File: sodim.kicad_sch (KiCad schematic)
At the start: 7 parts, among them J1 Edge_Conn_Bus_LPDDR5_testbed, J2 Edge_Connus_LPDDR5_testbed, U7 AT24CS01_SOT23

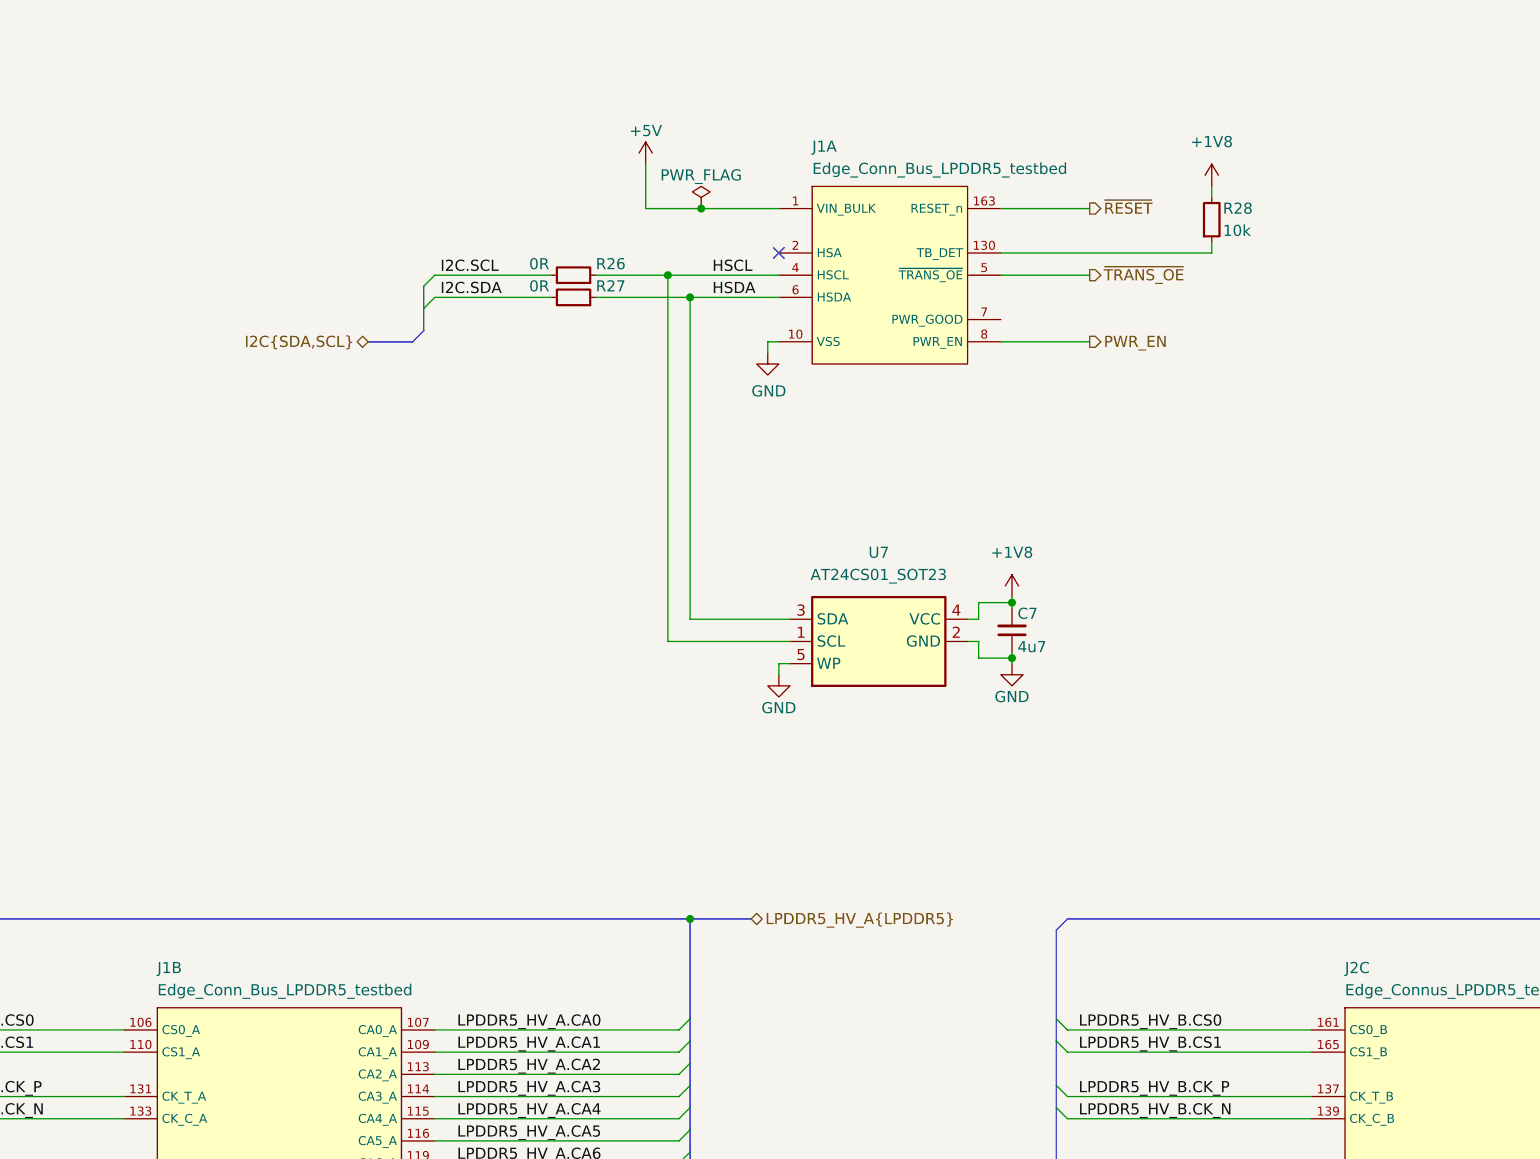
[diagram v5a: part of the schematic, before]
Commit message: [#52835] schematics: update translators pinout to for better package breakout
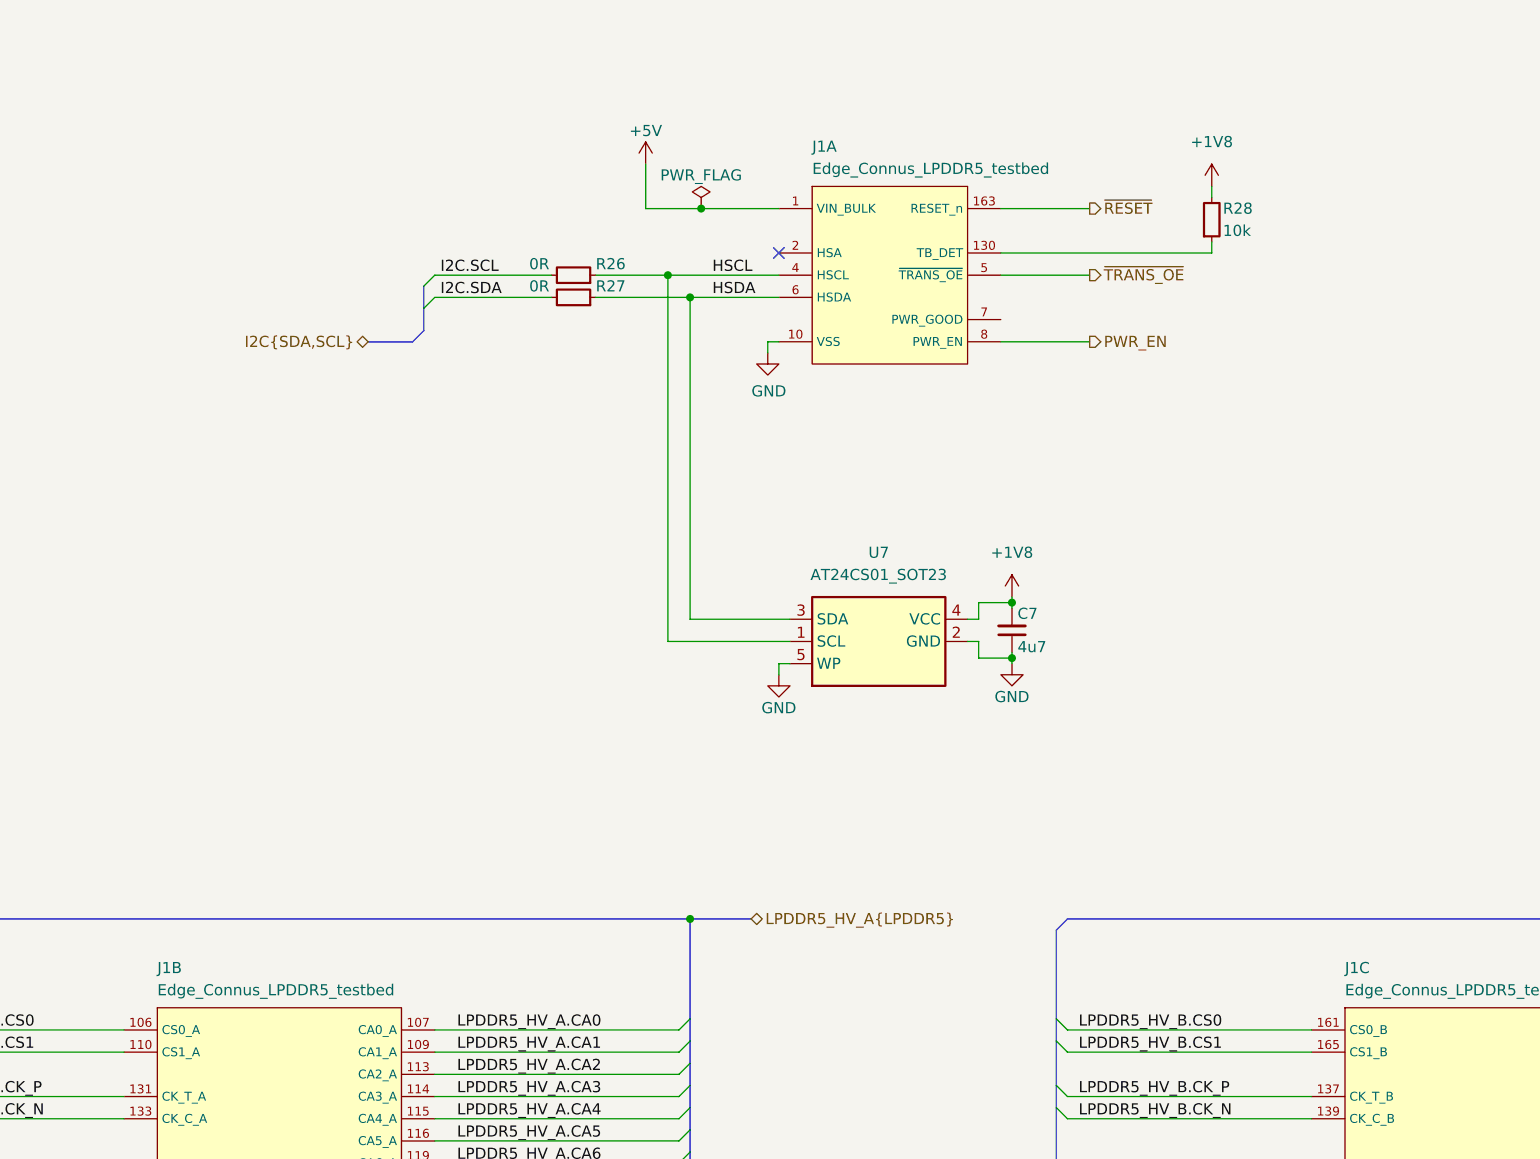
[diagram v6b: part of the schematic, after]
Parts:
- J1: value Edge_Conn_Bus_LPDDR5_testbed -> Edge_Connus_LPDDR5_testbed
- renumbered J2 to J1
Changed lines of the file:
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@@
       (effects (font (size 1.27 1.27)) (justify left bottom))
     )
-    (property "Value" "Edge_Conn_Bus_LPDDR5_testbed" (id 1) (at 121.92 139.7 0)
+    (property "Value" "Edge_Connus_LPDDR5_testbed" (id 1) (at 121.92 139.7 0)
       (effects (font (size 1.27 1.27)) (justify left bottom))
     )
@@
   (symbol (lib_id "antmicroMemoryConnectorsPCCardSockets:Edge_Conn_Bus_LPDDR5_testbed") (at 254 143.51 0) (unit 3)
     (in_bom yes) (on_board yes)
-    (property "Reference" "J2" (id 0) (at 257.81 137.16 0)
+    (property "Reference" "J1" (id 0) (at 257.81 137.16 0)
       (effects (font (size 1.27 1.27)) (justify left bottom))
     )
@@
       (effects (font (size 1.27 1.27)) (justify left bottom))
     )
-    (property "Value" "Edge_Conn_Bus_LPDDR5_testbed" (id 1) (at 196.85 45.72 0)
+    (property "Value" "Edge_Connus_LPDDR5_testbed" (id 1) (at 196.85 45.72 0)
       (effects (font (size 1.27 1.27)) (justify left bottom))
     )

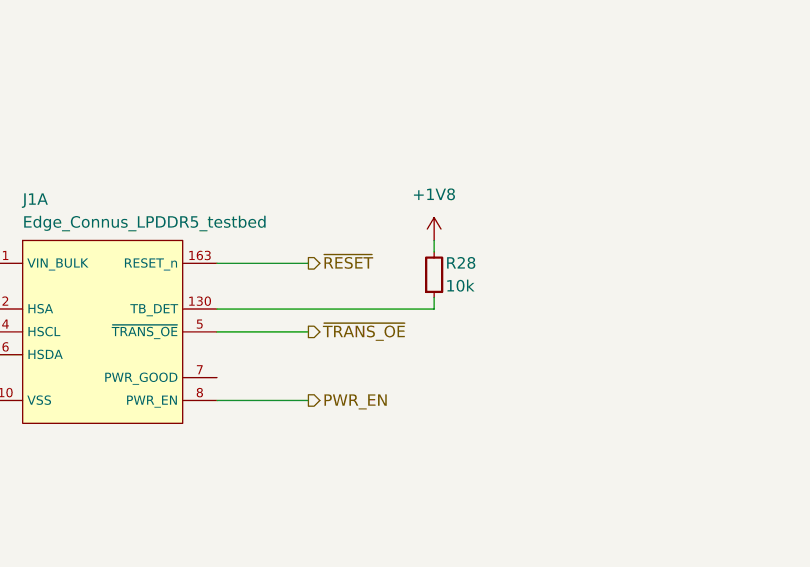
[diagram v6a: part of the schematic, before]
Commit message: [#52536] schematics: use voltage divider to detect pin
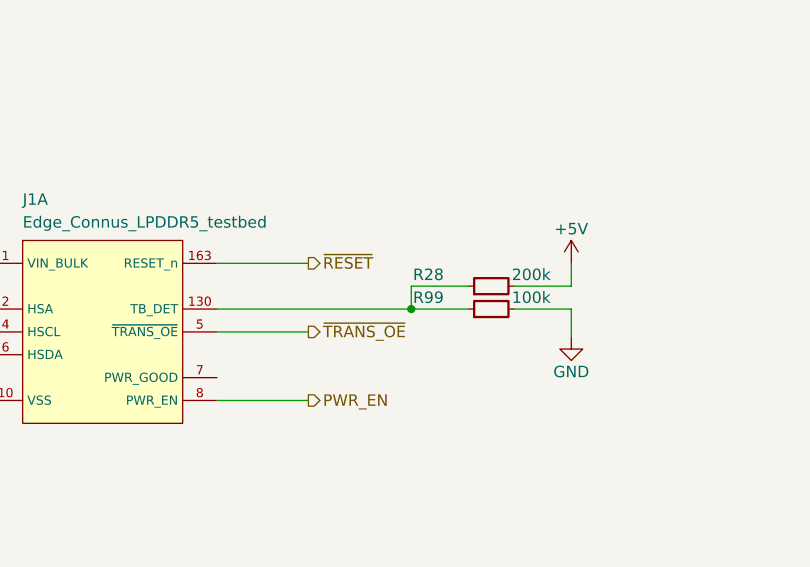
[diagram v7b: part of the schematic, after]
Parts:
- removed R28: R_10k_0402, antmicro-footprints:R_0402_1005Metric, symbol antmicroResistors0402:R_10k_0402
- added R28: R_200k_0402, antmicro-footprints:R_0402_1005Metric, symbol antmicroResistors0402:R_200k_0402
- added R99: R_100k_0402, antmicro-footprints:R_0402_1005Metric, symbol antmicroResistors0402:R_100k_0402
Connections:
- net +5V: now also R28.2
- net GND: now also R99.2
- net at J1.130 (TB_DET): now also R28.1, R99.1

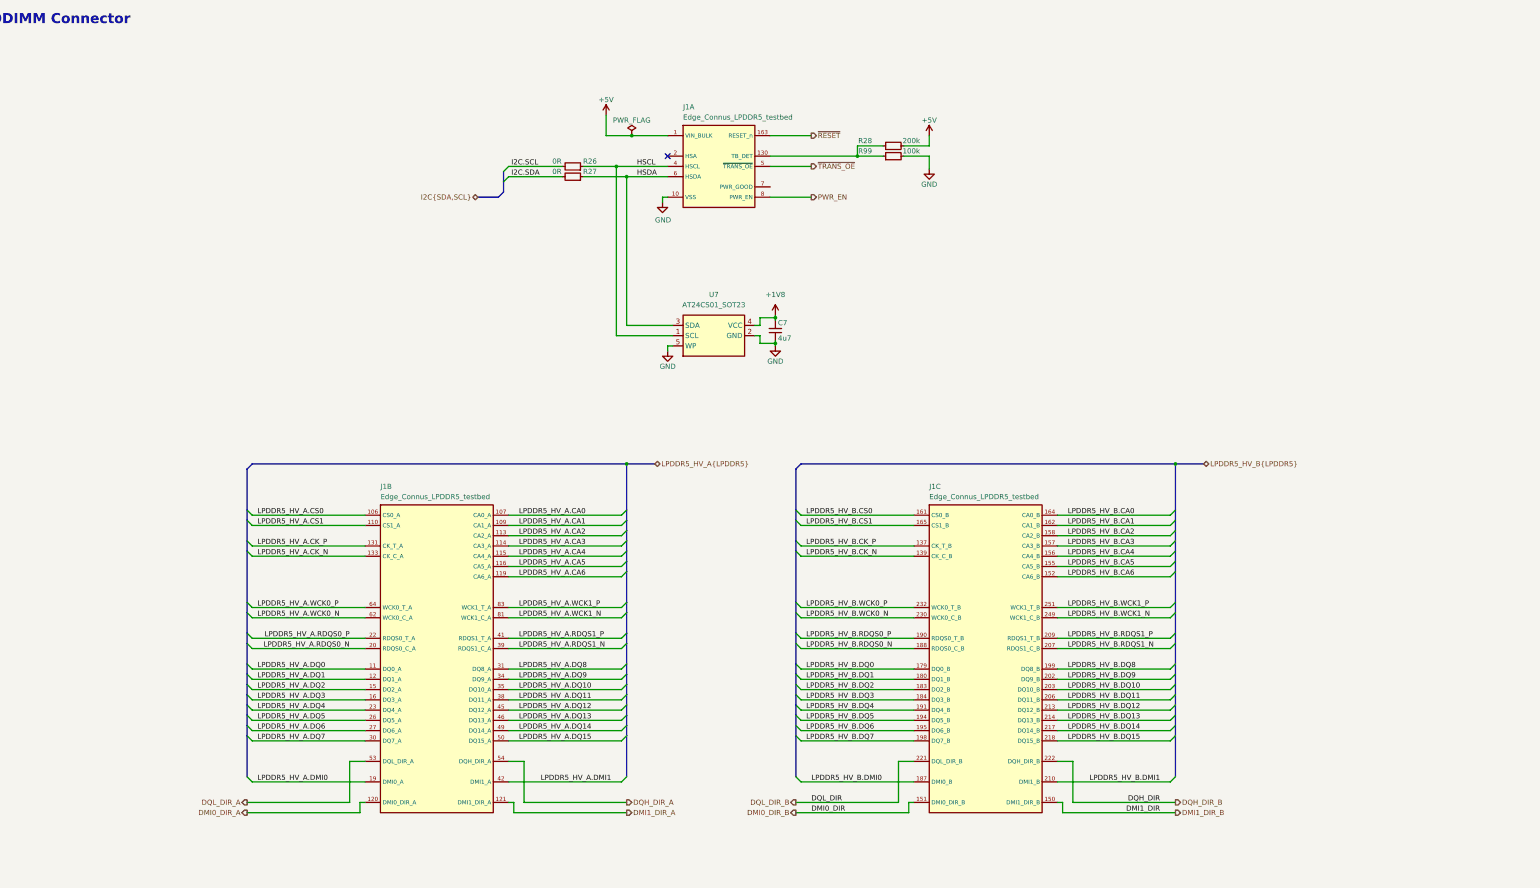
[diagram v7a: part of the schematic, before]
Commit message: [#52536] 52835: use resistors dividers instead of translators
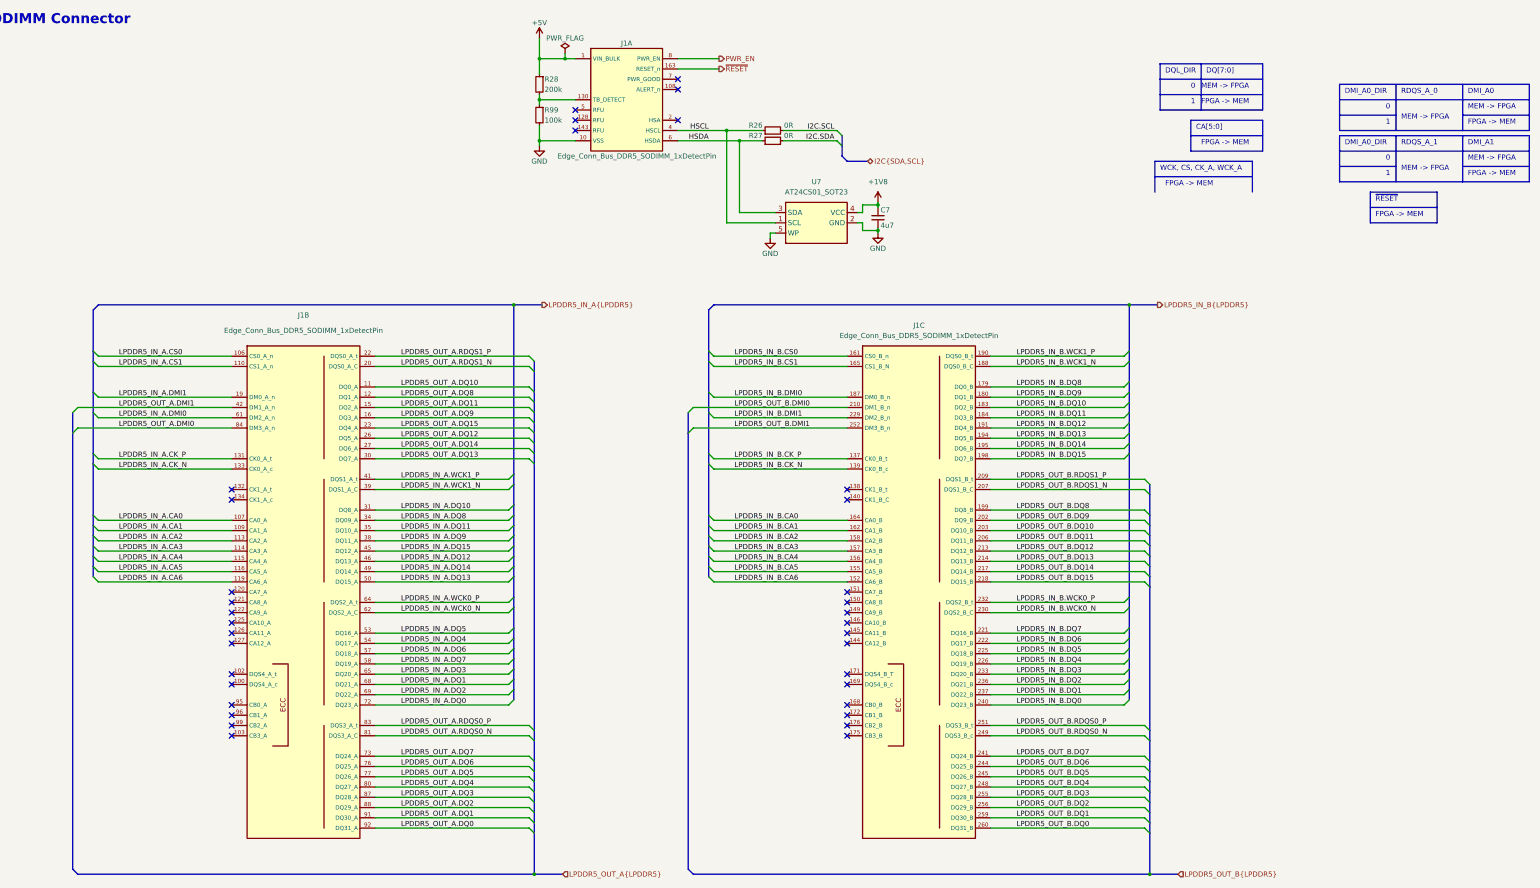
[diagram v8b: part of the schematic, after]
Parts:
- removed J1: Edge_Connus_LPDDR5_testbed, antmicro-footprints:Edge_Conn_Bus_DDR5_SODIMM, symbol antmicroMemoryConnectorsPCCardSockets:Edge_Conn_Bus_LPDDR5_testbed
- added J1: Edge_Conn_Bus_DDR5_SODIMM_1xDetectPin, antmicro-footprints:Edge_Conn_Bus_DDR5_SODIMM, symbol antmicroMemoryConnectorsPCCardSockets:Edge_Conn_Bus_DDR5_SODIMM_1xDetectPin
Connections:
- net +5V: now also R28.1, J1.1 (VIN_BULK), J1.3 (VIN_BULK); no longer R28.2
- net GND: now also J1.10 (VSS), J1.101 (VSS), J1.104 (VSS), J1.105 (VSS), J1.111 (VSS), J1.112 (VSS), J1.117 (VSS), J1.118 (VSS), J1.123 (VSS), J1.124 (VSS), J1.129 (VSS), J1.13 (VSS), J1.135 (VSS), J1.136 (VSS), J1.14 (VSS), J1.141 (VSS), J1.142 (VSS), J1.147 (VSS), J1.148 (VSS), J1.153 (VSS), J1.154 (VSS), J1.159 (VSS), J1.160 (VSS), J1.166 (VSS), J1.167 (VSS), J1.17 (VSS), J1.170 (VSS), J1.173 (VSS), J1.174 (VSS), J1.177 (VSS), J1.178 (VSS), J1.18 (VSS), J1.181 (VSS), J1.182 (VSS), J1.185 (VSS), J1.186 (VSS), J1.189 (VSS), J1.192 (VSS), J1.193 (VSS), J1.196 (VSS), J1.197 (VSS), J1.200 (VSS), J1.201 (VSS), J1.204 (VSS), J1.205 (VSS), J1.208 (VSS), J1.21 (VSS), J1.211 (VSS), J1.212 (VSS), J1.215 (VSS), J1.216 (VSS), J1.219 (VSS), J1.220 (VSS), J1.223 (VSS), J1.224 (VSS), J1.227 (VSS), J1.228 (VSS), J1.231 (VSS), J1.234 (VSS), J1.235 (VSS), J1.238 (VSS), J1.239 (VSS), J1.24 (VSS), J1.242 (VSS), J1.243 (VSS), J1.246 (VSS), J1.247 (VSS), J1.25 (VSS), J1.250 (VSS), J1.253 (VSS), J1.254 (VSS), J1.257 (VSS), J1.258 (VSS), J1.261 (VSS), J1.262 (VSS), J1.28 (VSS), J1.29 (VSS), J1.32 (VSS), J1.33 (VSS), J1.36 (VSS), J1.37 (VSS), J1.40 (VSS), J1.43 (VSS), J1.44 (VSS), J1.47 (VSS), J1.48 (VSS), J1.51 (VSS), J1.52 (VSS), J1.55 (VSS), J1.56 (VSS), J1.59 (VSS), J1.60 (VSS), J1.63 (VSS), J1.66 (VSS), J1.67 (VSS), J1.70 (VSS), J1.71 (VSS), J1.74 (VSS), J1.75 (VSS), J1.78 (VSS), J1.79 (VSS), J1.82 (VSS), J1.85 (VSS), J1.86 (VSS), J1.89 (VSS), J1.9 (VSS), J1.90 (VSS), J1.93 (VSS), J1.94 (VSS), J1.97 (VSS), J1.98 (VSS)
- net HSCL: now also J1.4 (HSCL)
- net HSDA: now also J1.6 (HSDA)
- net PWR_EN: now also J1.8 (PWR_EN)
- net ~{RESET}: now also J1.163 (RESET_n)
- net at R99.1: now also R28.2, J1.130 (TB_DETECT); no longer R28.1
- new net LPDDR5_IN_A.CA0: J1.107 (CA0_A)
- new net LPDDR5_IN_A.CA1: J1.109 (CA1_A)
- new net LPDDR5_IN_A.CA2: J1.113 (CA2_A)
- new net LPDDR5_IN_A.CA3: J1.114 (CA3_A)
- new net LPDDR5_IN_A.CA4: J1.115 (CA4_A)
- new net LPDDR5_IN_A.CA5: J1.116 (CA5_A)
- new net LPDDR5_IN_A.CA6: J1.119 (CA6_A)
- new net LPDDR5_IN_A.CK_N: J1.133 (CK0_A_c)
- new net LPDDR5_IN_A.CK_P: J1.131 (CK0_A_t)
- new net LPDDR5_IN_A.CS0: J1.106 (CS0_A_n)
- new net LPDDR5_IN_A.CS1: J1.110 (CS1_A_n)
- new net LPDDR5_IN_A.DMI0: J1.61 (DM2_A_n)
- new net LPDDR5_IN_A.DMI1: J1.19 (DM0_A_n)
- new net LPDDR5_IN_A.DQ0: J1.72 (DQ23_A)
- new net LPDDR5_IN_A.DQ1: J1.68 (DQ21_A)
- new net LPDDR5_IN_A.DQ10: J1.31 (DQ8_A)
- new net LPDDR5_IN_A.DQ11: J1.35 (DQ10_A)
- new net LPDDR5_IN_A.DQ12: J1.46 (DQ13_A)
- new net LPDDR5_IN_A.DQ13: J1.50 (DQ15_A)
- new net LPDDR5_IN_A.DQ14: J1.49 (DQ14_A)
- new net LPDDR5_IN_A.DQ15: J1.45 (DQ12_A)
- new net LPDDR5_IN_A.DQ2: J1.69 (DQ22_A)
- new net LPDDR5_IN_A.DQ3: J1.65 (DQ20_A)
- new net LPDDR5_IN_A.DQ4: J1.54 (DQ17_A)
- new net LPDDR5_IN_A.DQ5: J1.53 (DQ16_A)
- new net LPDDR5_IN_A.DQ6: J1.57 (DQ18_A)
- new net LPDDR5_IN_A.DQ7: J1.58 (DQ19_A)
- new net LPDDR5_IN_A.DQ8: J1.34 (DQ09_A)
- new net LPDDR5_IN_A.DQ9: J1.38 (DQ11_A)
- new net LPDDR5_IN_A.WCK0_N: J1.62 (DQS2_A_C)
- new net LPDDR5_IN_A.WCK0_P: J1.64 (DQS2_A_t)
- new net LPDDR5_IN_A.WCK1_N: J1.39 (DQS1_A_C)
- new net LPDDR5_IN_A.WCK1_P: J1.41 (DQS1_A_t)
- new net LPDDR5_IN_B.CA0: J1.164 (CA0_B)
- new net LPDDR5_IN_B.CA1: J1.162 (CA1_B)
- new net LPDDR5_IN_B.CA2: J1.158 (CA2_B)
- new net LPDDR5_IN_B.CA3: J1.157 (CA3_B)
- new net LPDDR5_IN_B.CA4: J1.156 (CA4_B)
- new net LPDDR5_IN_B.CA5: J1.155 (CA5_B)
- new net LPDDR5_IN_B.CA6: J1.152 (CA6_B)
- new net LPDDR5_IN_B.CK_N: J1.139 (CK0_B_c)
- new net LPDDR5_IN_B.CK_P: J1.137 (CK0_B_t)
- new net LPDDR5_IN_B.CS0: J1.161 (CS0_B_n)
- new net LPDDR5_IN_B.CS1: J1.165 (CS1_B_N)
- new net LPDDR5_IN_B.DMI0: J1.187 (DM0_B_n)
- new net LPDDR5_IN_B.DMI1: J1.229 (DM2_B_n)
- new net LPDDR5_IN_B.DQ0: J1.240 (DQ23_B)
- new net LPDDR5_IN_B.DQ1: J1.237 (DQ22_B)
- new net LPDDR5_IN_B.DQ10: J1.183 (DQ2_B)
- new net LPDDR5_IN_B.DQ11: J1.184 (DQ3_B)
- new net LPDDR5_IN_B.DQ12: J1.191 (DQ4_B)
- new net LPDDR5_IN_B.DQ13: J1.194 (DQ5_B)
- new net LPDDR5_IN_B.DQ14: J1.195 (DQ6_B)
- new net LPDDR5_IN_B.DQ15: J1.198 (DQ7_B)
- new net LPDDR5_IN_B.DQ2: J1.236 (DQ21_B)
- new net LPDDR5_IN_B.DQ3: J1.233 (DQ20_B)
- new net LPDDR5_IN_B.DQ4: J1.226 (DQ19_B)
- new net LPDDR5_IN_B.DQ5: J1.225 (DQ18_B)
- new net LPDDR5_IN_B.DQ6: J1.222 (DQ17_B)
- new net LPDDR5_IN_B.DQ7: J1.221 (DQ16_B)
- new net LPDDR5_IN_B.DQ8: J1.179 (DQ0_B)
- new net LPDDR5_IN_B.DQ9: J1.180 (DQ1_B)
- new net LPDDR5_IN_B.WCK0_N: J1.230 (DQS2_B_C)
- new net LPDDR5_IN_B.WCK0_P: J1.232 (DQS2_B_t)
- new net LPDDR5_IN_B.WCK1_N: J1.188 (DQS0_B_C)
- new net LPDDR5_IN_B.WCK1_P: J1.190 (DQS0_B_t)
- new net LPDDR5_OUT_A.DMI0: J1.84 (DM3_A_n)
- new net LPDDR5_OUT_A.DMI1: J1.42 (DM1_A_n)
- new net LPDDR5_OUT_A.DQ0: J1.92 (DQ31_A)
- new net LPDDR5_OUT_A.DQ1: J1.91 (DQ30_A)
- new net LPDDR5_OUT_A.DQ10: J1.11 (DQ0_A)
- new net LPDDR5_OUT_A.DQ11: J1.15 (DQ2_A)
- new net LPDDR5_OUT_A.DQ12: J1.26 (DQ5_A)
- new net LPDDR5_OUT_A.DQ13: J1.30 (DQ7_A)
- new net LPDDR5_OUT_A.DQ14: J1.27 (DQ6_A)
- new net LPDDR5_OUT_A.DQ15: J1.23 (DQ4_A)
- new net LPDDR5_OUT_A.DQ2: J1.88 (DQ29_A)
- new net LPDDR5_OUT_A.DQ3: J1.87 (DQ28_A)
- new net LPDDR5_OUT_A.DQ4: J1.80 (DQ27_A)
- new net LPDDR5_OUT_A.DQ5: J1.77 (DQ26_A)
- new net LPDDR5_OUT_A.DQ6: J1.76 (DQ25_A)
- new net LPDDR5_OUT_A.DQ7: J1.73 (DQ24_A)
- new net LPDDR5_OUT_A.DQ8: J1.12 (DQ1_A)
- new net LPDDR5_OUT_A.DQ9: J1.16 (DQ3_A)
- new net LPDDR5_OUT_A.RDQS0_N: J1.81 (DQS3_A_C)
- new net LPDDR5_OUT_A.RDQS0_P: J1.83 (DQS3_A_t)
- new net LPDDR5_OUT_A.RDQS1_N: J1.20 (DQS0_A_C)
- new net LPDDR5_OUT_A.RDQS1_P: J1.22 (DQS0_A_t)
- new net LPDDR5_OUT_B.DMI0: J1.210 (DM1_B_n)
- new net LPDDR5_OUT_B.DMI1: J1.252 (DM3_B_n)
- new net LPDDR5_OUT_B.DQ0: J1.260 (DQ31_B)
- new net LPDDR5_OUT_B.DQ1: J1.259 (DQ30_B)
- new net LPDDR5_OUT_B.DQ10: J1.203 (DQ10_B)
- new net LPDDR5_OUT_B.DQ11: J1.206 (DQ11_B)
- new net LPDDR5_OUT_B.DQ12: J1.213 (DQ12_B)
- new net LPDDR5_OUT_B.DQ13: J1.214 (DQ13_B)
- new net LPDDR5_OUT_B.DQ14: J1.217 (DQ14_B)
- new net LPDDR5_OUT_B.DQ15: J1.218 (DQ15_B)
- new net LPDDR5_OUT_B.DQ2: J1.256 (DQ29_B)
- new net LPDDR5_OUT_B.DQ3: J1.255 (DQ28_B)
- new net LPDDR5_OUT_B.DQ4: J1.248 (DQ27_B)
- new net LPDDR5_OUT_B.DQ5: J1.245 (DQ26_B)
- new net LPDDR5_OUT_B.DQ6: J1.244 (DQ25_B)
- new net LPDDR5_OUT_B.DQ7: J1.241 (DQ24_B)
- new net LPDDR5_OUT_B.DQ8: J1.199 (DQ8_B)
- new net LPDDR5_OUT_B.DQ9: J1.202 (DQ9_B)
- new net LPDDR5_OUT_B.RDQS0_N: J1.249 (DQS3_B_c)
- new net LPDDR5_OUT_B.RDQS0_P: J1.251 (DQS3_B_t)
- new net LPDDR5_OUT_B.RDQS1_N: J1.207 (DQS1_B_C)
- new net LPDDR5_OUT_B.RDQS1_P: J1.209 (DQS1_B_t)
- no-connect marks 1 -> 34
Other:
- note added: "0"
- note added: "1"
- note added: "CA[5:0]"
- note added: "DMI_A0"
- note added: "DMI_A0_DIR"
- note added: "DMI_A1"
- note added: "DQL_DIR"
- note added: "DQ[7:0]"
- note added: "FPGA -> MEM"
- note added: "MEM -> FPGA"
- note added: "RDQS_A_0"
- note added: "RDQS_A_1"
- note added: "WCK, CS, CK_A, WCK_A"
- note added: "~{RESET}"
- moved on the sheet: C7, R26, R27, R28, R99, U7
